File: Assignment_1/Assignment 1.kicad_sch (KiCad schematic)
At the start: 17 parts, among them J4 Jack-DC, J5 Screw_Terminal_01x02, J6 Screw_Terminal_01x02, SW1 SW_SP3T, T2 TY-311P, U1 LM7805_TO220, U2 LM317_TO-220, X1 AC Jack

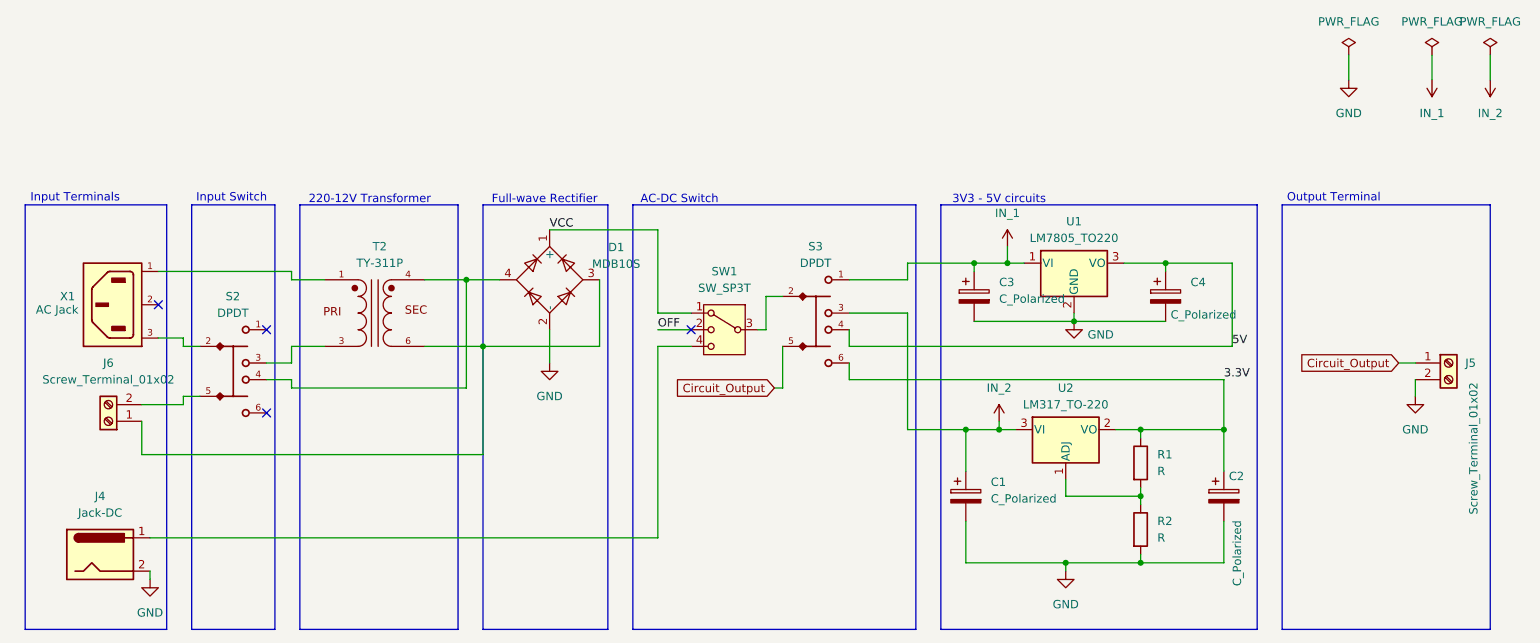
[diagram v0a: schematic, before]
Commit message: Add custom components for all assignments
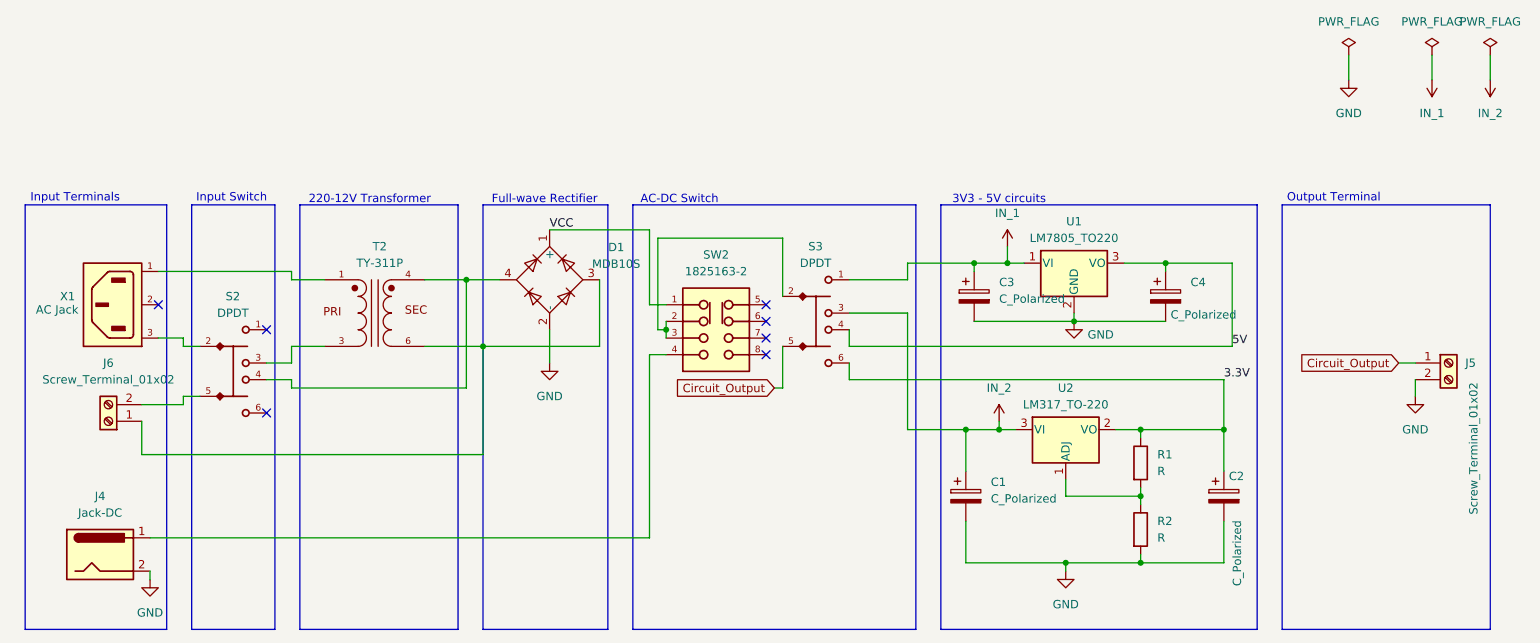
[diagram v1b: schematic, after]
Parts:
- removed SW1: SW_SP3T, DP3T:SW_1825163-2, symbol Switch:SW_SP3T
- added SW2: 1825163-2, 1825163-2:SW_1825163-2, symbol 1825163-2:1825163-2
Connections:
- net VCC: now also SW2.1
- net at J4.1: now also SW2.4
- net at S3.2: now also SW2.2, SW2.3
- no-connect marks 4 -> 7

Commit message: Update layout of all assignments
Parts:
- removed D1: MDB10S, Package_SO:TSSOP-4_4.4x5mm_P4mm, symbol Diode_Bridge:MDB10S
- added D2: B40C3x00-2200A, Diode_THT:Diode_Bridge_32.0x5.6x17.0mm_P10.0mm_P7.5mm, symbol Diode_Bridge:B40C3x00-2200A
- SW2: footprint 1825163-2:SW_1825163-2 -> DP3T:SW_1825163-2
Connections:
- net GND: now also D2.3
- net VCC: now also D2.2
- net at S2.4, T2.4: now also D2.1 (-)
- net at J6.1 (Pin_1), T2.6: now also D2.4 (+)
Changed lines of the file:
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@@
+	)
+	(junction
+		(at 104.14 69.85)
+		(diameter 0)
+		(color 0 0 0 0)
 	)
 	(junction
@@
 	)
 	(junction
+		(at 116.84 62.23)
+		(diameter 0)
+		(color 0 0 0 0)
+	)
+	(junction
 		(at 134.62 77.47)
 		(diameter 0)
@@
 	)
 	(junction
-		(at 104.14 69.85)
-		(diameter 0)
-		(color 0 0 0 0)
-	)
-	(junction
 		(at 207.01 92.71)
 		(diameter 0)
@@
 	(wire
 		(pts
+			(xy 104.14 69.85) (xy 104.14 86.36)
+		)
+		(stroke
+			(width 0)
+			(type default)
+		)
+	)
+	(wire
+		(pts
 			(xy 152.4 72.39) (xy 152.4 63.5)
 		)
@@
 	(wire
 		(pts
-			(xy 104.14 69.85) (xy 104.14 86.36)
-		)
-		(stroke
-			(width 0)
-			(type default)
-		)
-	)
-	(wire
-		(pts
 			(xy 185.42 91.44) (xy 185.42 92.71)
 		)
@@
 		(pts
 			(xy 54.61 96.52) (xy 106.68 96.52)
+		)
+		(stroke
+			(width 0)
+			(type default)
+		)
+	)
+	(wire
+		(pts
+			(xy 116.84 62.23) (xy 116.84 63.5)
 		)
 		(stroke
@@
 				(justify right)
 				(hide yes)
+			)
+		)
+	)
+	(symbol
+		(lib_id "Diode_Bridge:B40C3x00-2200A")
+		(at 116.84 69.85 0)
+		(unit 1)
+		(exclude_from_sim no)
+		(in_bom yes)
+		(on_board yes)
+		(dnp no)
+		(fields_autoplaced yes)
+		(property "Reference" "D2"
+			(at 132.08 63.4298 0)
+			(effects
+				(font
+					(size 1.27 1.27)
+				)
+			)
+		)
+		(property "Value" "B40C3x00-2200A"
+			(at 132.08 65.9698 0)
+			(effects
+				(font
+					(size 1.27 1.27)
+				)
+			)
+		)
+		(property "Footprint" "Diode_THT:Diode_Bridge_32.0x5.6x17.0mm_P10.0mm_P7.5mm"
+			(at 120.65 66.675 0)
+			(effects
+				(font
+					(size 1.27 1.27)
+				)
+				(justify left)
+				(hide yes)
+			)
+		)
+		(property "Datasheet" "https://diotec.com/tl_files/diotec/files/pdf/datasheets/b40c3700"
+			(at 116.84 69.85 0)
+			(effects
+				(font
+					(size 1.27 1.27)
+				)
+				(hide yes)
+			)
+		)
+		(property "Description" "Silicon Bridge Rectifier, 40V Vrms, 2.2A If, pins=-AA+, SIL-package"
+			(at 116.84 69.85 0)
+			(effects
+				(font
+					(size 1.27 1.27)
+				)
+				(hide yes)
+			)
+		)
+		(pin "3"
+		)
+		(pin "2"
+		)
+		(pin "1"
+		)
+		(pin "4"
+		)
+		(instances
+			(project ""
+				(path "/3372f59d-e2fb-4a2a-b342-548a4f8e5741"
+					(reference "D2")
+					(unit 1)
+				)
 			)
 		)
@@
 	)
 	(symbol
-		(lib_id "Diode_Bridge:MDB10S")
-		(at 116.84 69.85 90)
-		(unit 1)
-		(exclude_from_sim no)
-		(in_bom yes)
-		(on_board yes)
-		(dnp no)
-		(fields_autoplaced yes)
-		(property "Reference" "D1"
-			(at 127 64.8968 90)
-			(effects
-				(font
-					(size 1.27 1.27)
-				)
-			)
-		)
-		(property "Value" "MDB10S"
-			(at 127 67.4368 90)
-			(effects
-				(font
-					(size 1.27 1.27)
-				)
-			)
-		)
-		(property "Footprint" "Package_SO:TSSOP-4_4.4x5mm_P4mm"
-			(at 116.84 69.85 0)
-			(effects
-				(font
-					(size 1.27 1.27)
-				)
-				(hide yes)
-			)
-		)
-		(property "Datasheet" "https://www.onsemi.com/pub/Collateral/MDB8S-D.PDF"
-			(at 116.84 69.85 0)
-			(effects
-				(font
-					(size 1.27 1.27)
-				)
-				(hide yes)
-			)
-		)
-		(property "Description" "Single-Phase Bridge Rectifier, 700V Vrms, 1A If, TSSOP-4"
-			(at 116.84 69.85 0)
-			(effects
-				(font
-					(size 1.27 1.27)
-				)
-				(hide yes)
-			)
-		)
-		(pin "4"
-		)
-		(pin "3"
-		)
-		(pin "1"
-		)
-		(pin "2"
-		)
-		(instances
-			(project "Assignment 1"
-				(path "/3372f59d-e2fb-4a2a-b342-548a4f8e5741"
-					(reference "D1")
-					(unit 1)
-				)
-			)
-		)
-	)
-	(symbol
 		(lib_id "1825163-2:1825163-2")
 		(at 142.24 78.74 0)
@@
 			)
 		)
-		(property "Footprint" "1825163-2:SW_1825163-2"
+		(property "Footprint" "DP3T:SW_1825163-2"
 			(at 142.24 78.74 0)
 			(effects
